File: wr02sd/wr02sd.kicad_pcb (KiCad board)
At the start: 2 copper layers, 39.6 x 49.8 mm, 34 parts, among them CON1 SD_Card, P1 THT_Male_P_1x15, P2 USB_A, P3 THT_Male_P_1x15, P4 POWER_5V, SW1 Flash, SW2 Reset, U1 CH340G, U2 LM3940IMP-3.3, U3 ESP-13-WROOM-02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

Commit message: PCB Artworking is progressing..
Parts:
- CON1: value SD_Card -> Micro_SD_Card
- moved CON1 0.13 mm to (162.8, 123.1)
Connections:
- CON1 pad 1: /GPIO15(CD) -> Net-(CON1-Pad1)
- CON1 pad 10: Net-(CON1-Pad10) -> (no net)
- CON1 pad 11: Net-(CON1-Pad11) -> (no net)
- CON1 pad 12: GND -> (no net)
- CON1 pad 13: GND -> (no net)
- CON1 pad 2: /GPIO13(MOSI) -> /GPIO15(CD)
- CON1 pad 3: GND -> /GPIO13(MOSI)
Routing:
- net VCC: track 11.4 -> 86.6 mm, vias 1 -> 9
- net /GPIO16: track 0.00 -> 64.3 mm, vias 0 -> 1
- net /GPIO5: track 0.00 -> 58.3 mm, vias 0 -> 1
- net /GPIO14(CK): track 0.00 -> 55.1 mm, vias 0 -> 3
- net /GPIO2: track 0.00 -> 52.6 mm, vias 0 -> 4
- net /nRST: track 0.00 -> 51.7 mm, vias 0 -> 4
- net /GPIO4: track 0.00 -> 51.5 mm, vias 0 -> 1
- net /GPIO15(CD): track 0.00 -> 48.3 mm, vias 0 -> 9
- net /GPIO12(MISO): track 0.00 -> 47.2 mm, vias 0 -> 5
- net /GPIO13(MOSI): track 0.00 -> 47.1 mm, vias 0 -> 6
- net /RS232_RX: track 0.00 -> 41.4 mm, vias 0 -> 3
- net /RS232_TX: track 0.00 -> 37.1 mm, vias 0 -> 3
- net VDD: track 0.00 -> 34.4 mm, vias 0 -> 2
- net /USB_D-: track 0.00 -> 30.5 mm, vias 0 -> 2
- net /USB_D+: track 0.00 -> 30.1 mm, vias 0 -> 2
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
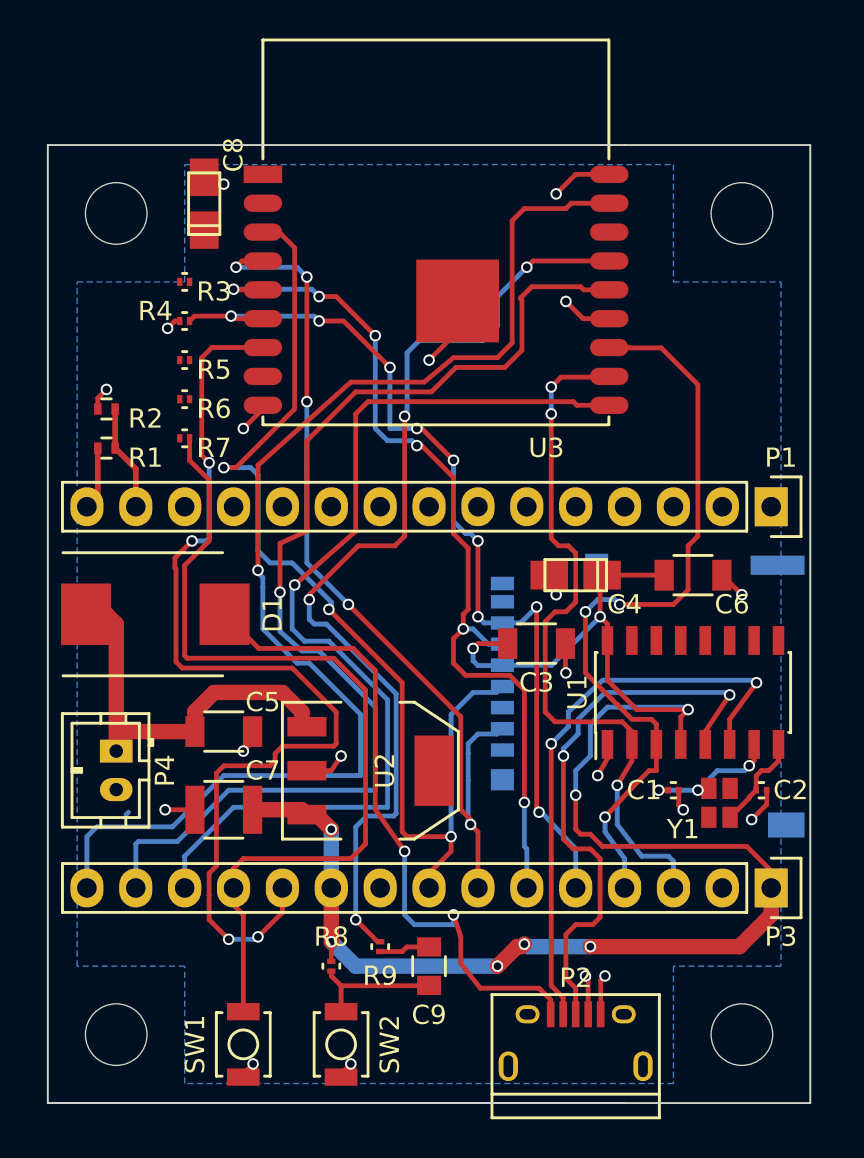
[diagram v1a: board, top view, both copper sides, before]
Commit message: PCB Artworking the first is done.
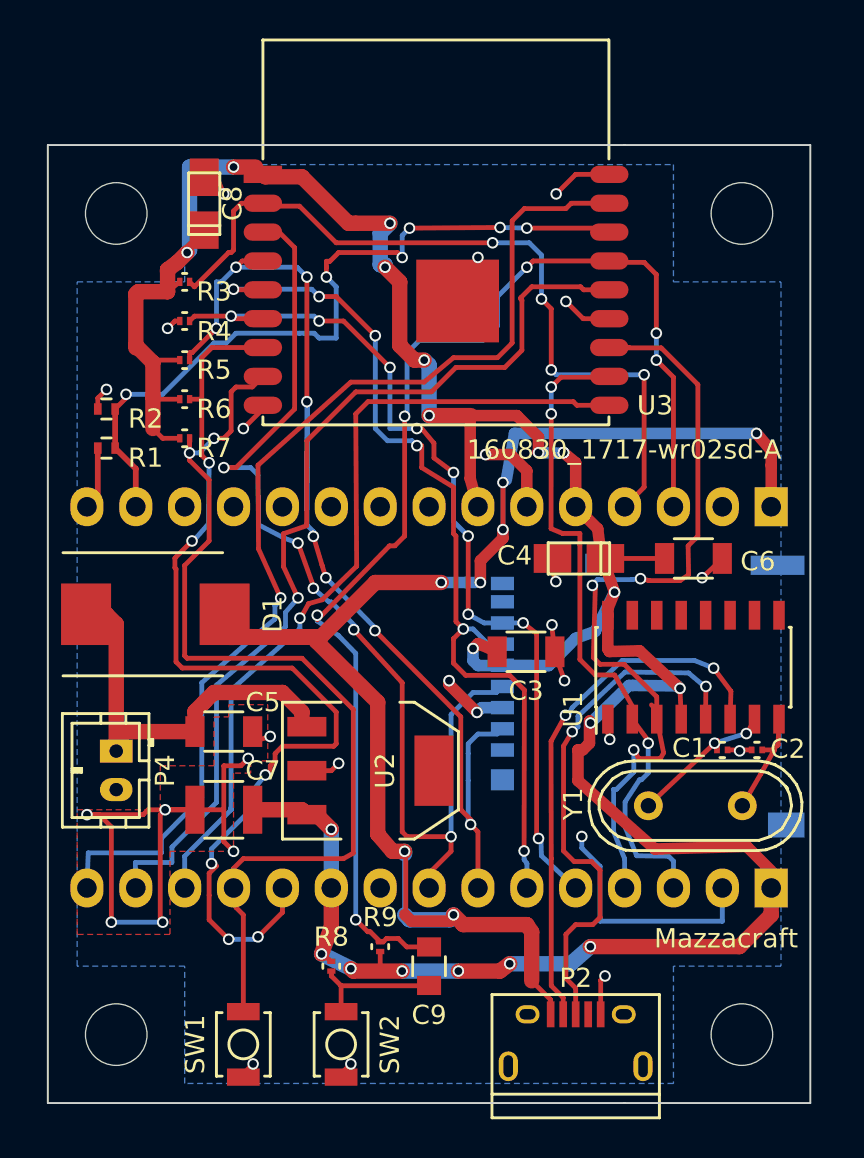
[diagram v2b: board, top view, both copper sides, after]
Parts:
- P1, P3: moved to B.Cu
- Y1: footprint wroom02:smd_xtal -> Crystals:Crystal_HC49-U_Vertical
- moved C1 3.29 mm to (170.9, 125.2)
- moved C2 2.11 mm to (172.7, 125.2), turned to 180 degrees
- moved Y1 1.43 mm to (169.5, 128.1)
- moved U1 1.31 mm to (169.4, 120.9)
- moved C4 0.88 mm to (163.5, 115.2)
- moved C6 0.87 mm to (169.4, 115.2)
- moved C3 0.70 mm to (160.7, 120.1)
- turned P1 to 90 degrees
- turned P3 to 90 degrees
- turned R9 to 90 degrees
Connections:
- C9 pad 2: Net-(C9-Pad2) -> /nRST
- P2 pad 4: GND -> Net-(P2-Pad4)
- R9 pad 1: /nRST -> VCC
- R9 pad 2: Net-(C9-Pad2) -> /nRST
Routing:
- net VCC: track 86.6 -> 154.9 mm, vias 9 -> 20
- net VDD: track 34.4 -> 84.0 mm, vias 2 -> 7
- net GND: track 34.2 -> 81.6 mm, vias 20 -> 28
- net /EN: track 0.00 -> 40.9 mm, vias 0 -> 4
- net /ADC: track 5.52 -> 39.4 mm, vias 0 -> 6
- net /nRST: track 51.7 -> 65.9 mm, vias 4 -> 6
- net /GPIO12(MISO): track 47.2 -> 58.3 mm, vias 5 -> 8
- net /GPIO4: track 51.5 -> 42.7 mm
- net /GPIO5: track 58.3 -> 49.8 mm
- net /GPIO16: track 64.3 -> 56.2 mm
- net /GPIO0: track 45.4 -> 51.2 mm, vias 0 -> 2
- net Net-(C9-Pad2): track 2.64 -> 0.00 mm
- net /USB_D-: track 30.5 -> 27.9 mm
- net /RS232_TX: track 37.1 -> 34.8 mm
- net /RS232_RX: track 41.4 -> 43.5 mm
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- added copper zone on F.Cu, net GND
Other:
- board text added: "160830_1717-wr02sd-A"
- board text added: "Mazzacraft"

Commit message: CH340G Placement test crossing on sdcard receptacle
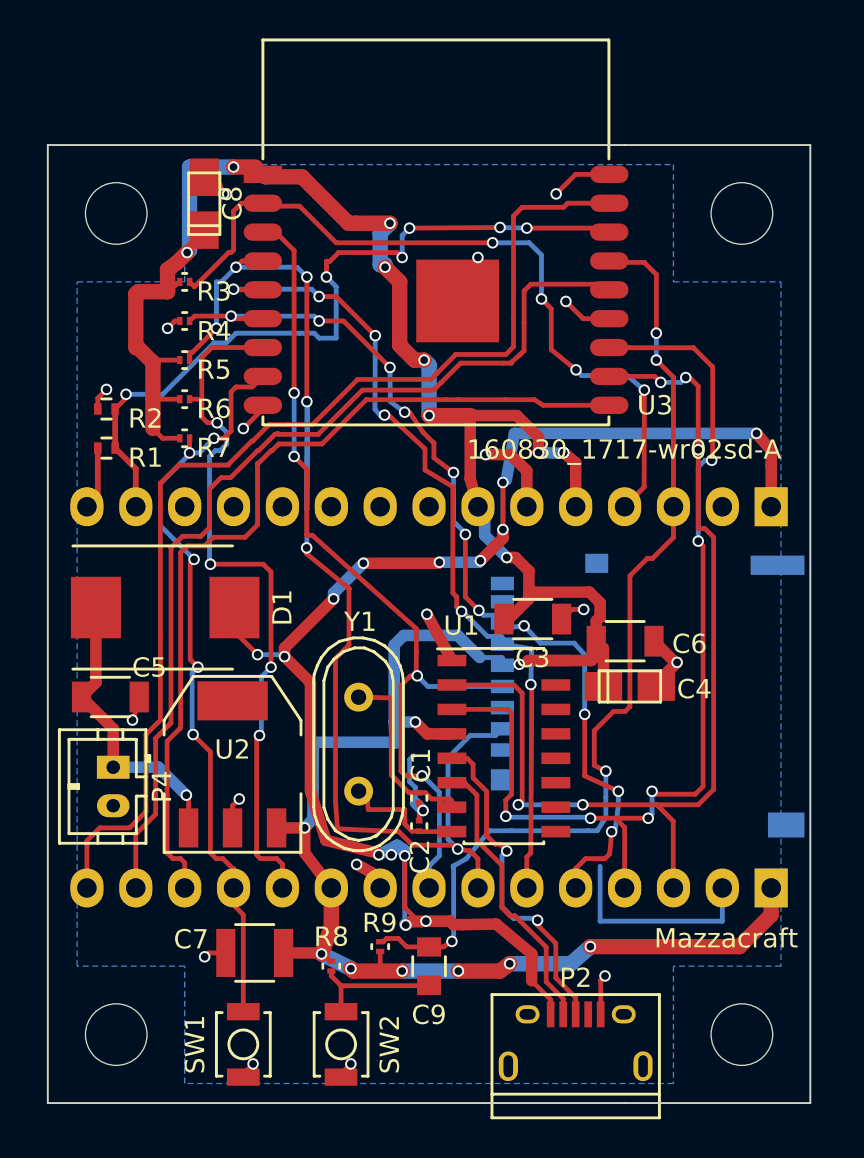
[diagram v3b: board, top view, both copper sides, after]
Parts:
- moved C2 18.0 mm to (155.2, 129.1), turned to 90 degrees
- moved Y1 17.8 mm to (152.0, 124.9), turned to 270 degrees
- moved C1 15.9 mm to (155.2, 127.7), turned to 270 degrees
- moved U1 10.7 mm to (159.6, 125.0), turned to 0 degrees
- moved C7 7.61 mm to (146.6, 135.7)
- moved U2 7.17 mm to (145.5, 125.9), turned to 0 degrees
- moved C4 7.16 mm to (166.1, 121.9), turned to 180 degrees
- moved C5 6.16 mm to (139.1, 122.4)
- moved C6 5.58 mm to (165.9, 119.5)
- moved C3 1.74 mm to (161.1, 118.4)
- moved P4 0.85 mm to (139.3, 126.1)
- moved D1 0.62 mm to (142.0, 117.8)
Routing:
- net GND: track 81.6 -> 52.9 mm, vias 28 -> 19
- net /RS232_TX: track 34.8 -> 51.5 mm, vias 3 -> 5
- net /nRST: track 65.9 -> 51.0 mm, vias 6 -> 4
- net /GPIO2: track 51.7 -> 37.2 mm, vias 6 -> 4
- net /USB_D-: track 27.9 -> 15.0 mm, vias 2 -> 0
- net /USB_D+: track 28.2 -> 17.5 mm
- net /GPIO0: track 51.2 -> 40.5 mm, vias 2 -> 5
- net /RS232_RX: track 43.5 -> 53.5 mm, vias 3 -> 6
- net /GPIO14(CK): track 54.7 -> 47.1 mm, vias 5 -> 4
- net /GPIO12(MISO): track 58.3 -> 64.2 mm, vias 8 -> 6
- net +5V: track 21.5 -> 16.1 mm, vias 0 -> 1
- net VCC: track 154.9 -> 150.9 mm, vias 20 -> 19
- net /GPIO4: track 42.7 -> 46.1 mm, vias 1 -> 0
- net /GPIO13(MOSI): track 47.1 -> 43.8 mm
- net VDD: track 84.0 -> 81.1 mm, vias 7 -> 14
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- removed copper zone on F.Cu, net GND
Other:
- rule trace_min: 0.1 -> 0

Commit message: Testing done.
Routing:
- net GND: track 52.9 -> 71.8 mm, vias 19 -> 22
- net /nRST: track 51.0 -> 55.9 mm, vias 4 -> 6
- net /GPIO14(CK): track 47.1 -> 49.0 mm
- net /GPIO12(MISO): track 64.2 -> 62.4 mm, vias 6 -> 8
- net /USB_D+: track 17.5 -> 18.4 mm
- net Net-(C2-Pad1): track 6.41 -> 5.57 mm
- net VCC: track 150.9 -> 151.5 mm
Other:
- board text added: "Flash"
- board text added: "Reset"

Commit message: Satisfy design
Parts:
- moved C2 9.98 mm to (156.4, 119.2), turned to 270 degrees
- moved C4 6.27 mm to (170.8, 126.1)
- moved C6 4.81 mm to (169.4, 122.8), turned to 90 degrees
- moved C1 4.33 mm to (156.4, 123.5), turned to 90 degrees
- moved Y1 3.79 mm to (153.5, 121.4), turned to 90 degrees
- moved U1 3.78 mm to (163.0, 123.3), turned to 270 degrees
- moved C3 1.97 mm to (163.0, 118.1)
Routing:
- net GND: track 71.8 -> 47.9 mm, vias 22 -> 21
- net VCC: track 151.5 -> 174.6 mm, vias 19 -> 21
- net /RS232_TX: track 51.5 -> 32.7 mm, vias 5 -> 2
- net /RS232_RX: track 53.5 -> 36.3 mm, vias 6 -> 4
- net /USB_D-: track 15.4 -> 21.8 mm, vias 0 -> 2
- net /GPIO14(CK): track 49.0 -> 55.3 mm, vias 4 -> 3
- net /USB_D+: track 18.4 -> 24.5 mm
- net /GPIO12(MISO): track 62.4 -> 58.0 mm
- net /GPIO13(MOSI): track 43.8 -> 45.9 mm
- net Net-(C1-Pad1): track 9.73 -> 8.63 mm
- net VDD: track 81.1 -> 80.0 mm, vias 14 -> 12
- net /GPIO15(CD): track 49.3 -> 48.2 mm, vias 11 -> 6
- net Net-(C2-Pad1): track 5.57 -> 6.10 mm
- net /GPIO2: track 37.2 -> 36.7 mm
- net /GPIO0: vias 5 -> 4

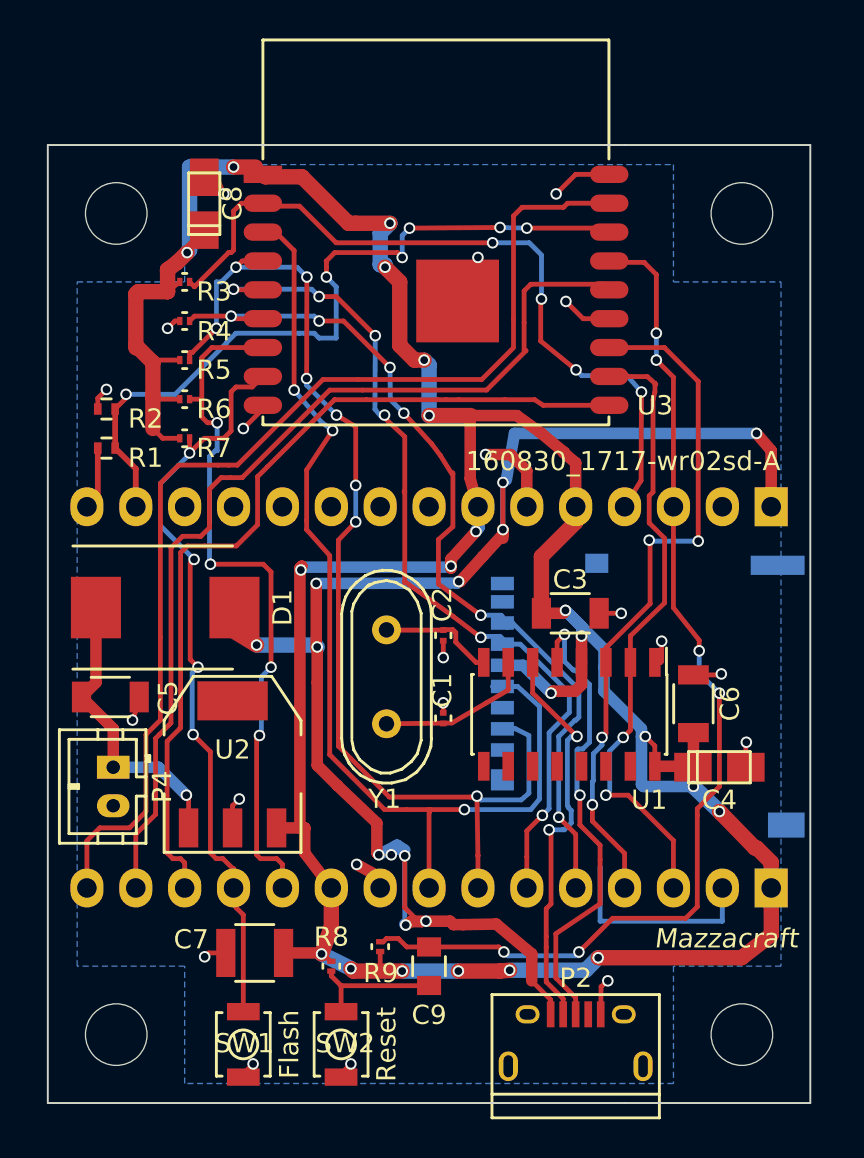
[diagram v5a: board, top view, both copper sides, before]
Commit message: Footprint was fit in to the ordered parts
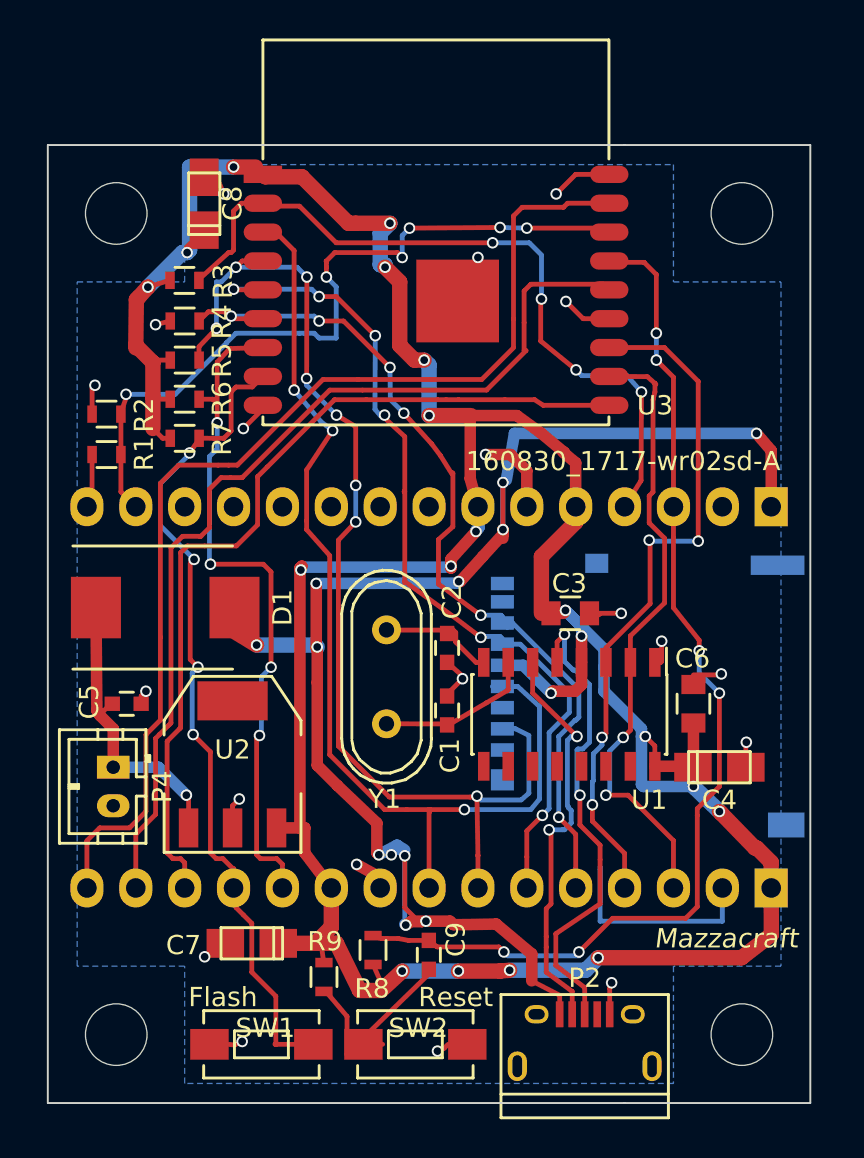
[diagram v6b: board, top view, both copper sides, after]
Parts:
- C1, C2: footprint Capacitors_SMD:C_0201 -> Capacitors_SMD:C_0603
- C3, C6: footprint Capacitors_SMD:C_1206 -> Capacitors_SMD:C_0805
- C5: footprint Capacitors_SMD:C_1206 -> Capacitors_SMD:C_0603
- C7: footprint Capacitors_SMD:C_1210 -> Capacitors_Tantalum_SMD:TantalC_SizeS_EIA-3216
- C9: footprint Capacitors_SMD:C_0805 -> Capacitors_SMD:C_0603
- R1, R2: footprint Resistors_SMD:R_0402 -> Resistors_SMD:R_0603
- R3, R4, R5, R6, R7, R8, R9: footprint Resistors_SMD:R_0201 -> Resistors_SMD:R_0603
- SW1, SW2: footprint Buttons_Switches_SMD:SW_SPST_B3U-1000P -> Buttons_Switches_SMD:SW_SPST_EVQPE1
- moved SW2 3.86 mm to (155.0, 140.5), turned to 180 degrees
- moved SW1 0.94 mm to (147.0, 140.5), turned to 0 degrees
- moved C5 0.92 mm to (140.0, 122.8)
- moved C2 0.68 mm to (156.6, 119.9)
- moved R8 0.68 mm to (150.2, 137.0)
- moved C9 0.59 mm to (155.7, 135.8)
- moved C7 0.52 mm to (146.5, 135.2), turned to 0 degrees
- moved P2 0.47 mm to (163.8, 140.5)
- moved C1 0.45 mm to (156.6, 123.1)
- moved R9 0.41 mm to (152.8, 135.6)
- moved R1 0.34 mm to (138.9, 109.8)
- moved R2 0.27 mm to (138.9, 107.7)
- moved R3 0.08 mm to (143.0, 100.8)
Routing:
- net Net-(C9-Pad1): track 6.90 -> 11.0 mm
- net /GPIO0: track 40.5 -> 44.2 mm
- net /GPIO2: track 36.7 -> 35.7 mm
- net GND: track 47.9 -> 47.1 mm, vias 21 -> 20
- net /EN: track 39.6 -> 38.8 mm
- net VCC: track 174.6 -> 174.2 mm, vias 21 -> 20

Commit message: 更新
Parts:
- D1: footprint Diodes_SMD:DO-214AB -> Diodes_SMD:DO-214BA
- P2: footprint Connect:USB_Micro-B -> USB_Micro-B
- moved D1 2.72 mm to (139.4, 118.7), turned to 90 degrees
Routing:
- net /GPIO15(CD): track 47.9 -> 61.3 mm, vias 6 -> 7
- net /GPIO13(MOSI): track 45.9 -> 54.2 mm, vias 6 -> 5
- net VDD: track 80.5 -> 86.4 mm, vias 12 -> 14
- net /GPIO14(CK): track 55.3 -> 52.1 mm, vias 3 -> 5
- net /GPIO12(MISO): track 57.7 -> 60.2 mm
- net +5V: track 15.8 -> 13.5 mm
- net /ADC: track 39.3 -> 38.3 mm
- net VCC: track 174.2 -> 173.5 mm
- net /USB_D-: track 22.1 -> 21.5 mm
- net /GPIO0: track 44.2 -> 44.7 mm
